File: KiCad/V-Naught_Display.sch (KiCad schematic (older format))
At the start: 28 parts, among them J1 USB_B_Micro, J2 I2C Header 1, J3 Conn_01x03, J4 Conn_01x02, J5 SWD Header, J6 I2C Header 2, SW1 SW_SPST, SW2 SW_SPST, SW3 SW_SPST, SW4 SW_SPST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

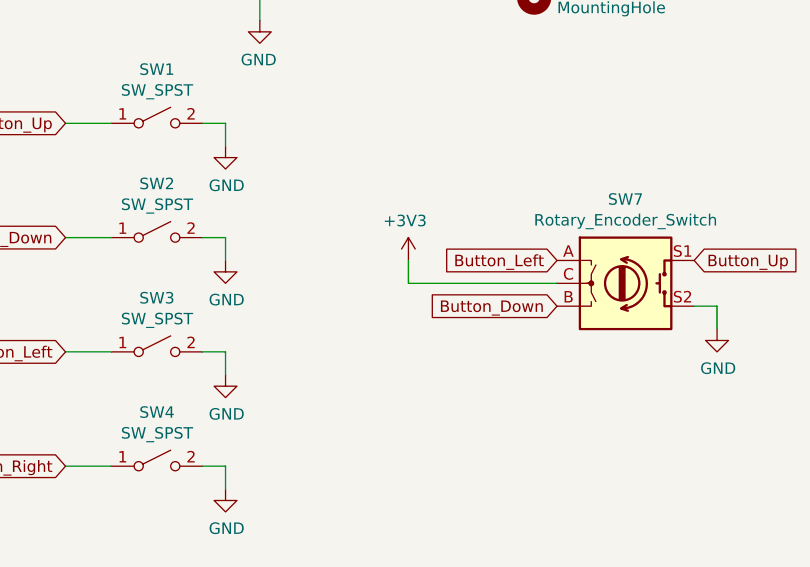
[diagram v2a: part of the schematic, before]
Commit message: Encoder Common pin change from 3v3 to Ground
Need to change encoder center pin to Ground (from 3V3) to allow for pullups to work for pin change detection.
Also, adding working configs for both the Encoder and Button options
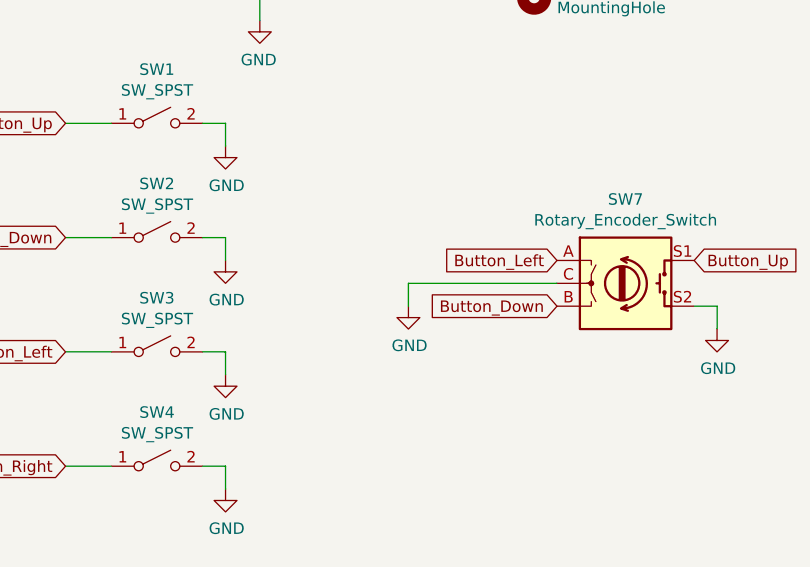
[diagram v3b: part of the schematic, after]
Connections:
- net +3V3: no longer SW7.C
- net GND: now also SW7.C
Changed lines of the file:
@@
 Wire Wire Line
 	5950 3800 5300 3800
-Wire Wire Line
-	5300 3800 5300 3700
-$Comp
-L power:+3V3 #PWR0123
-U 1 1 5E248221
-P 5300 3700
-F 0 "#PWR0123" H 5300 3550 50  0001 C CNN
-F 1 "+3V3" H 5315 3873 50  0000 C CNN
-F 2 "" H 5300 3700 50  0001 C CNN
-F 3 "" H 5300 3700 50  0001 C CNN
-	1    5300 3700
-	-1   0    0    -1
-$EndComp
 $Comp
 L Switch:SW_SPST SW6
@@
 Wire Wire Line
 	4600 1200 4600 1400
+$Comp
+L power:GND #PWR?
+U 1 1 5E58C340
+P 5300 3900
+F 0 "#PWR?" H 5300 3650 50  0001 C CNN
+F 1 "GND" H 5305 3727 50  0000 C CNN
+F 2 "" H 5300 3900 50  0001 C CNN
+F 3 "" H 5300 3900 50  0001 C CNN
+	1    5300 3900
+	1    0    0    -1
+$EndComp
+Wire Wire Line
+	5300 3900 5300 3800
 $EndSCHEMATC

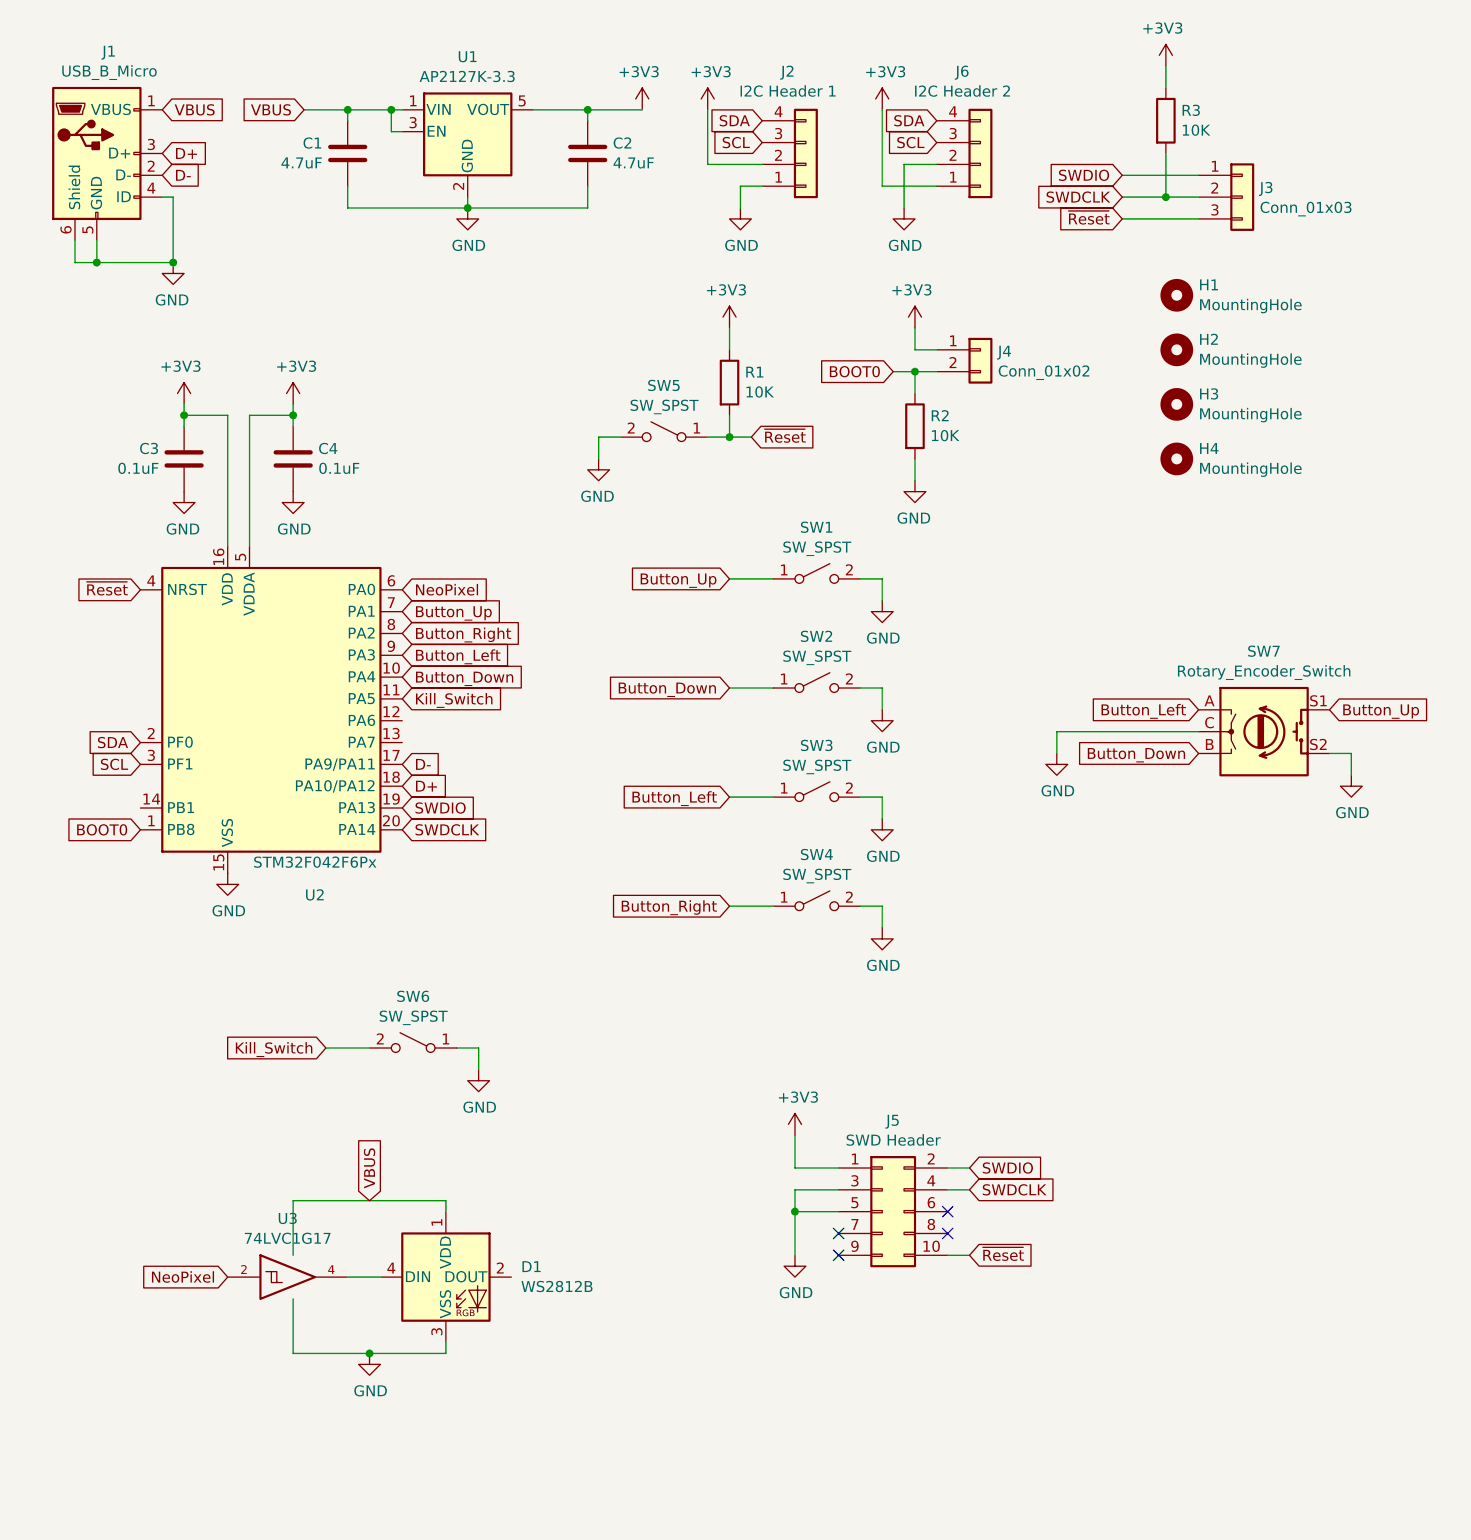
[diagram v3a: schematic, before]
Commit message: Widen to allow for screw mounting on all 4 sides.
2 screws were deemed insufficient ... =P
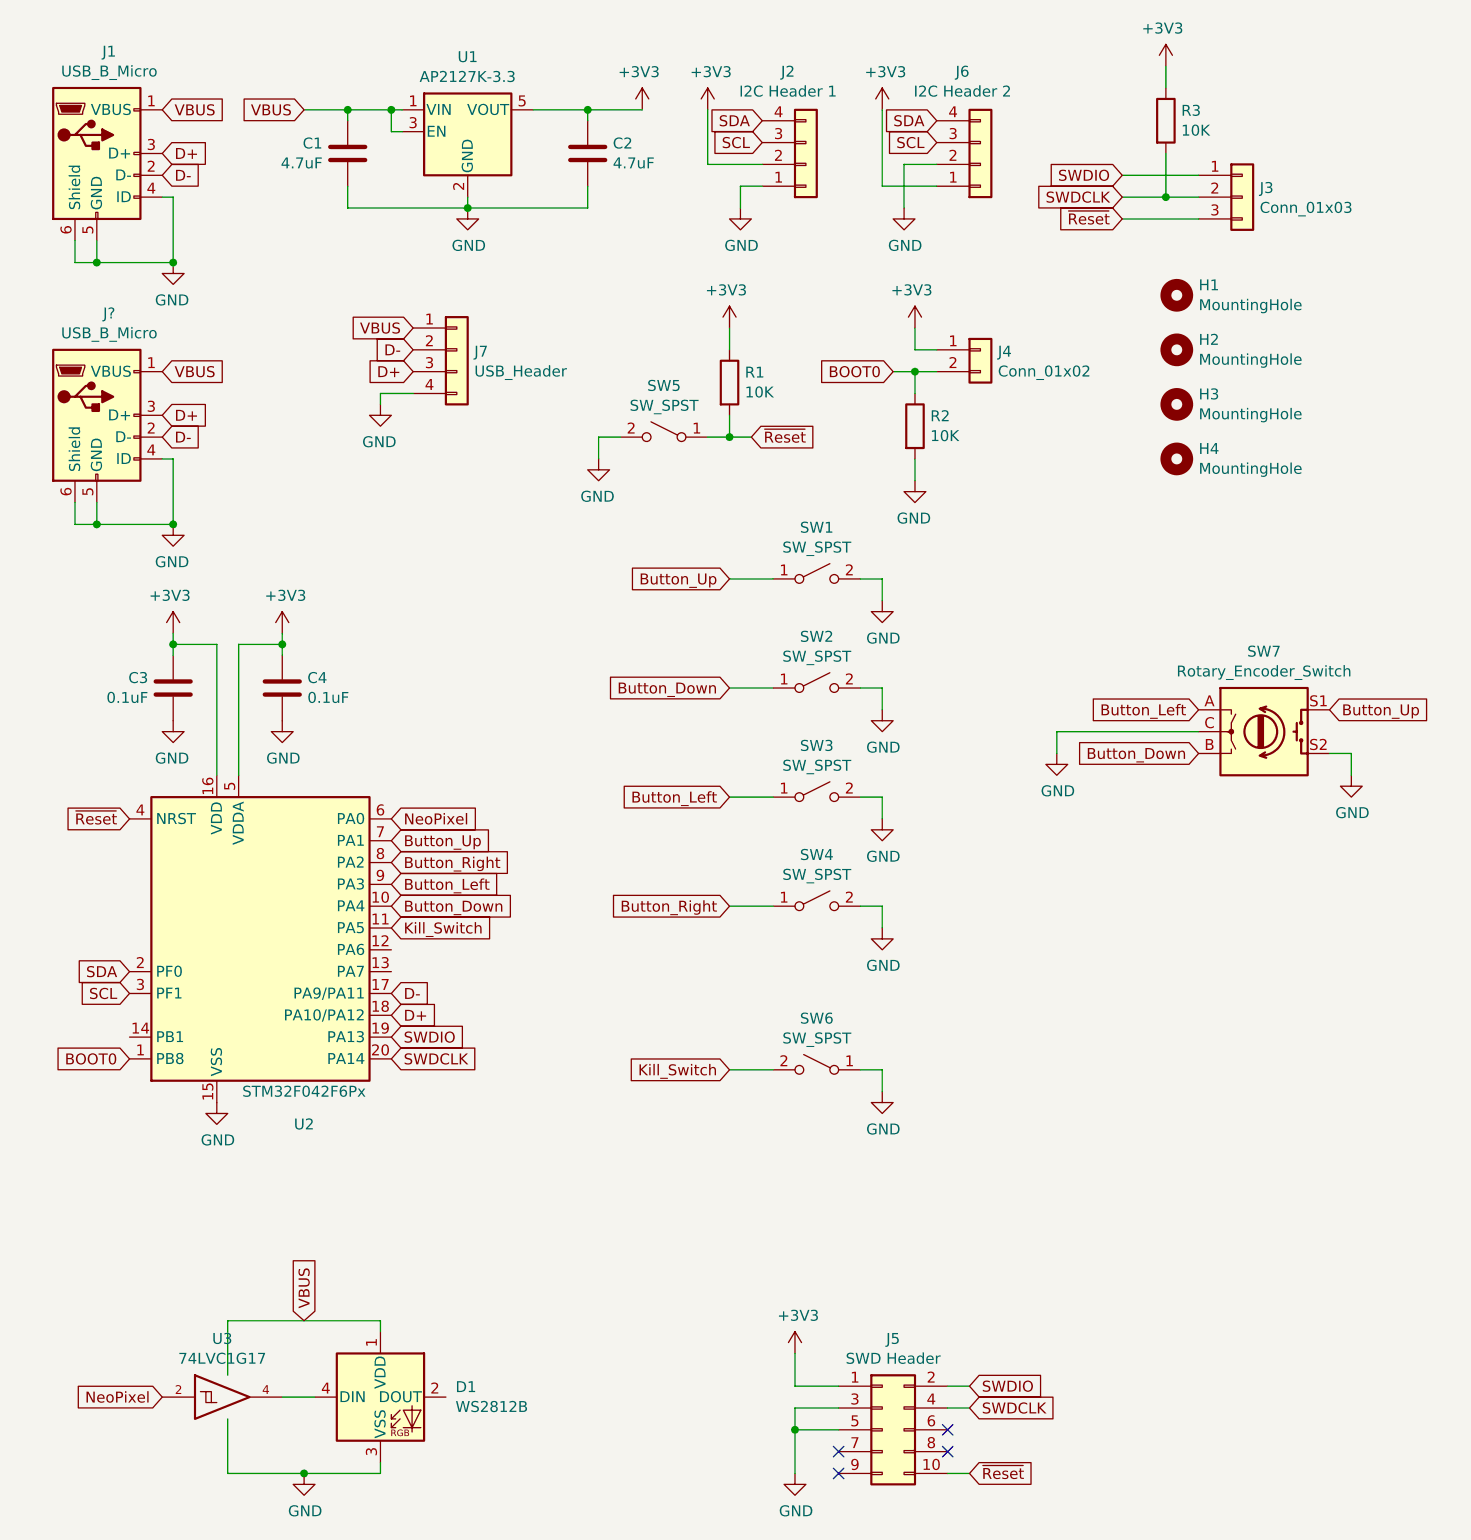
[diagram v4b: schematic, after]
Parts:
- added J7: USB_Header, TRA_KiCad_Footprints:01x04_unpopulated, symbol Connector_Generic:Conn_01x04
- added J?: USB_B_Micro, Connector_USB:USB_Micro-B_Molex-105017-0001, symbol Connector:USB_B_Micro
- SW7: footprint TRA_KiCad_Footprints:EN11 Encoder -> TRA_KiCad_Footprints:EN11_Encoder
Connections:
- net D+: now also J7.3 (Pin_3), J?.3 (D+)
- net D-: now also J7.2 (Pin_2), J?.2 (D-)
- net GND: now also J7.4 (Pin_4), J?.4 (ID), J?.5 (GND), J?.6 (Shield)
- net VCC: now also J7.1 (Pin_1), J?.1 (VBUS)
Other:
- moved on the sheet: C3, C4, D1, J5, SW6, U2, U3
